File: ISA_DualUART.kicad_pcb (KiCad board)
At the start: 2 copper layers, 176.5 x 90.2 mm, 74 parts, among them J1 ISA BUS, J10 Parallel Port, J2 ADDR_IRQ, J3 UART1_SEL, J4 UART2_SEL, J6 Serial 2 IDC, J7 Serial 1 DB9, J9 Parport IRQ Select, U1 74LS138, U11 74LS30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

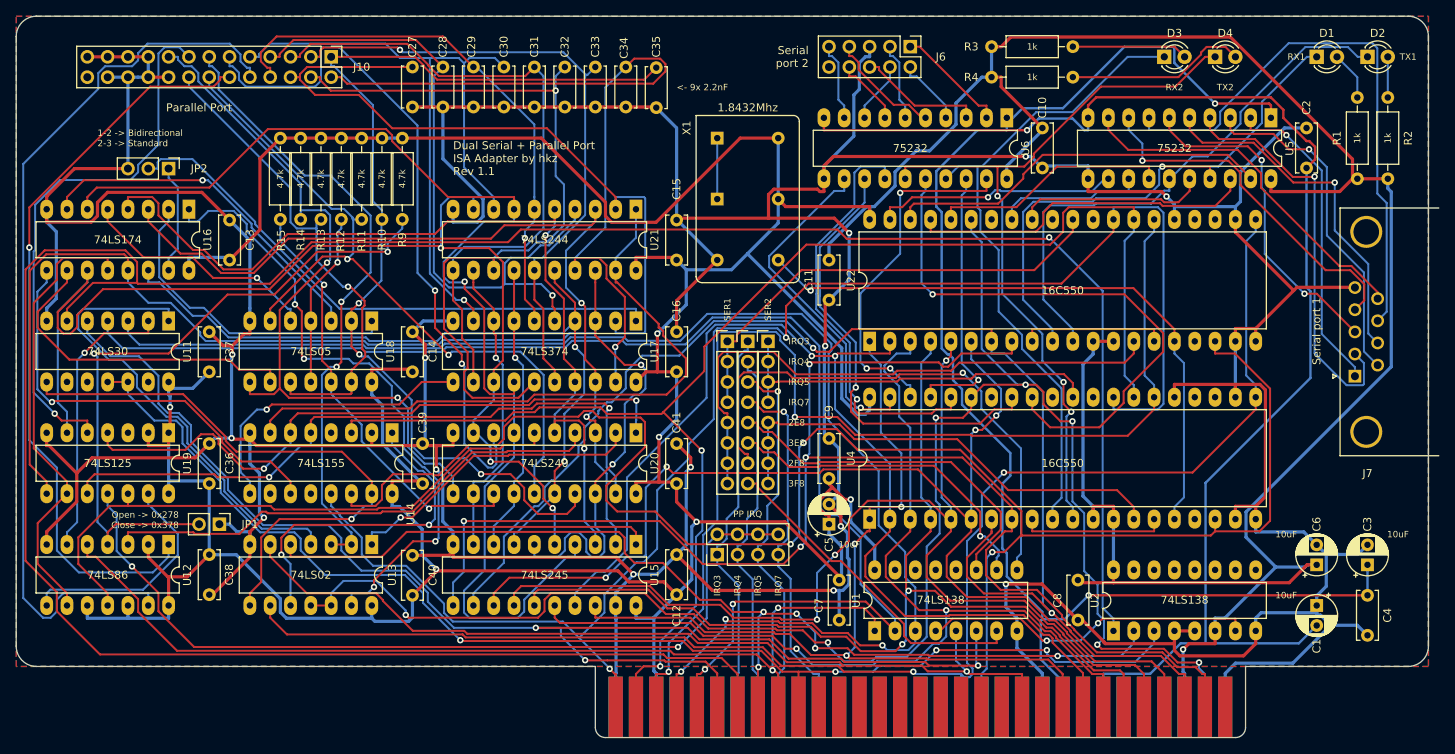
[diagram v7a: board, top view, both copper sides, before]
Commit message: Rerouted, now serial connector has shield to gnd
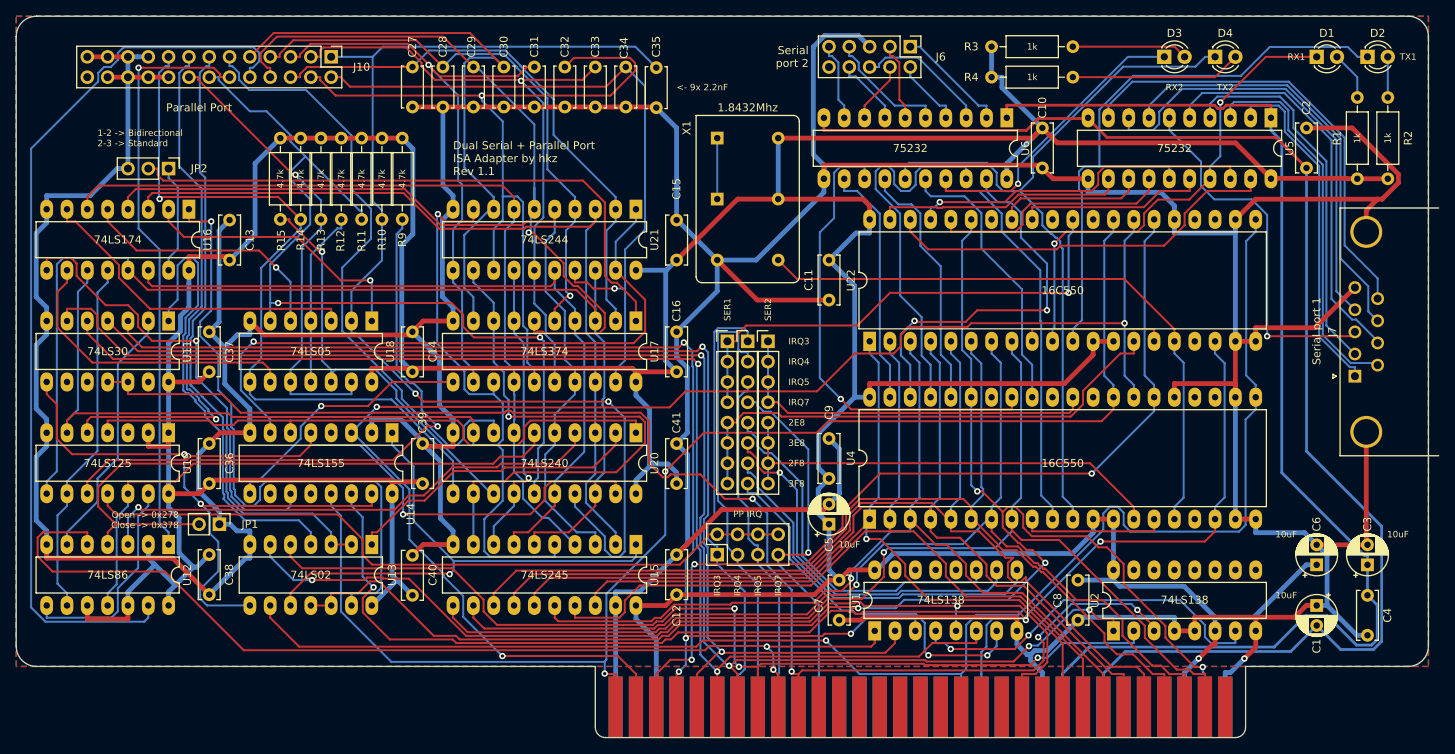
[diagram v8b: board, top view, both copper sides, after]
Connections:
- J7 pad 0: (no net) -> GND
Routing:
- net /A6: track 336.5 -> 183.4 mm, vias 1 -> 4
- net VCC: track 765.0 -> 648.5 mm, vias 7 -> 1
- net /PARPORT_BD2: track 152.1 -> 104.1 mm, vias 1 -> 0
- net /~IOW: track 216.0 -> 172.5 mm
- net /D7: track 183.0 -> 141.9 mm, vias 4 -> 1
- net /D6: track 173.5 -> 135.2 mm, vias 2 -> 1
- net /~RTS_2: track 72.0 -> 35.3 mm, vias 1 -> 0
- net /PARPORT_BD7: track 38.1 -> 71.4 mm
- net /A0: track 197.7 -> 168.7 mm
- net /A2: track 141.6 -> 112.9 mm, vias 2 -> 3
- net /D1: track 136.7 -> 108.6 mm, vias 2 -> 0
- net /A3: track 175.3 -> 150.1 mm, vias 3 -> 4
- net /A4: track 172.3 -> 147.9 mm
- net /PARPORT_BD4: track 166.5 -> 143.0 mm, vias 2 -> 0
- net /~CTS_2: track 53.5 -> 31.7 mm, vias 1 -> 0
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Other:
- net class POWER: trace_width 0.4 -> 0.6
- net class POWR_SMALL: trace_width 0.3 -> 0.35
